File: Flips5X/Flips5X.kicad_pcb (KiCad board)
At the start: 2 copper layers, 80 x 75 mm, 13 parts, among them CN1 Conn_02x30_Odd_Even, CN2 UFP2810, CN3 UFP2810, U1 FP2800A, U2 FP2800A

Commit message: introducing Flips5X concept
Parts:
- added C3: 0U1, Capacitors_SMD:C_0805_HandSoldering, F.Cu at (142.9, 130.2)
- added CNX1: UFP2810, Own:Pin_Header_Angle_Shrouded_2x05_Pitch2.54mm, F.Cu at (152.4, 144.8)
- added CNX2: Conn_02x20_Odd_Even, Socket_Strips:Socket_Strip_Straight_2x20_Pitch2.54mm, B.Cu at (159.4, 88.3)
- added U3: FP2800A, Housings_DIP:DIP-40_W15.24mm_Socket, F.Cu at (139.1, 89.5)
- moved REF** 80.5 mm to (221.1, 112.2)
- moved REF** 74.4 mm to (209.6, 141.0)
- moved REF*** 54.2 mm to (196.8, 131.4)
- moved REF** 40.3 mm to (168.9, 178.4)
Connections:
- net Net-(CN1-Pad1) renamed /SY1
- net Net-(CN1-Pad10) renamed /SY10
- net Net-(CN1-Pad11) renamed /SY11
- net Net-(CN1-Pad12) renamed /SY12
- net Net-(CN1-Pad13) renamed /SY13
- net Net-(CN1-Pad14) renamed /SY14
- net Net-(CN1-Pad15) renamed /SY15
- net Net-(CN1-Pad16) renamed /SY16
- net Net-(CN1-Pad17) renamed /SY17
- net Net-(CN1-Pad18) renamed /SY18
- net Net-(CN1-Pad19) renamed /SY19
- net Net-(CN1-Pad2) renamed /SY2
- net Net-(CN1-Pad20) renamed /SY20
- net Net-(CN1-Pad21) renamed /RY1
- net Net-(CN1-Pad22) renamed /RY2
- net Net-(CN1-Pad23) renamed /RY3
- net Net-(CN1-Pad24) renamed /RY4
- net Net-(CN1-Pad25) renamed /RY5
- net Net-(CN1-Pad26) renamed /RY6
- net Net-(CN1-Pad27) renamed /RY7
- net Net-(CN1-Pad28) renamed /RY8
- net Net-(CN1-Pad29) renamed /RY9
- net Net-(CN1-Pad3) renamed /SY3
- net Net-(CN1-Pad30) renamed /RY10
- net Net-(CN1-Pad31) renamed /RY11
- net Net-(CN1-Pad32) renamed /RY12
- net Net-(CN1-Pad33) renamed /RY13
- net Net-(CN1-Pad34) renamed /RY14
- net Net-(CN1-Pad35) renamed /RY15
- net Net-(CN1-Pad36) renamed /RY16
- net Net-(CN1-Pad37) renamed /RY17
- net Net-(CN1-Pad38) renamed /RY18
- net Net-(CN1-Pad39) renamed /RY19
- net Net-(CN1-Pad4) renamed /SY4
- net Net-(CN1-Pad40) renamed /RY20
- net Net-(CN1-Pad5) renamed /SY5
- net Net-(CN1-Pad6) renamed /SY6
- net Net-(CN1-Pad7) renamed /SY7
- net Net-(CN1-Pad8) renamed /SY8
- net Net-(CN1-Pad9) renamed /SY9
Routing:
- net /X3: track 0.00 -> 20.8 mm
- net /X14: track 0.00 -> 20.8 mm
- net /X1: track 0.00 -> 20.8 mm
- net /X9: track 0.00 -> 20.8 mm
- net /X8: track 0.00 -> 20.8 mm
- net /X7: track 0.00 -> 20.8 mm
- net /X6: track 0.00 -> 20.8 mm
- net /X5: track 0.00 -> 20.8 mm
- net /X4: track 0.00 -> 20.8 mm
- net /X2: track 0.00 -> 20.8 mm
- net /X13: track 0.00 -> 20.8 mm
- net /X12: track 0.00 -> 20.8 mm
- net /X11: track 0.00 -> 20.8 mm
- net /X10: track 0.00 -> 20.8 mm
- net /X23: track 0.00 -> 8.78 mm
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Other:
- board size 80 x 75 mm -> 97 x 75 mm

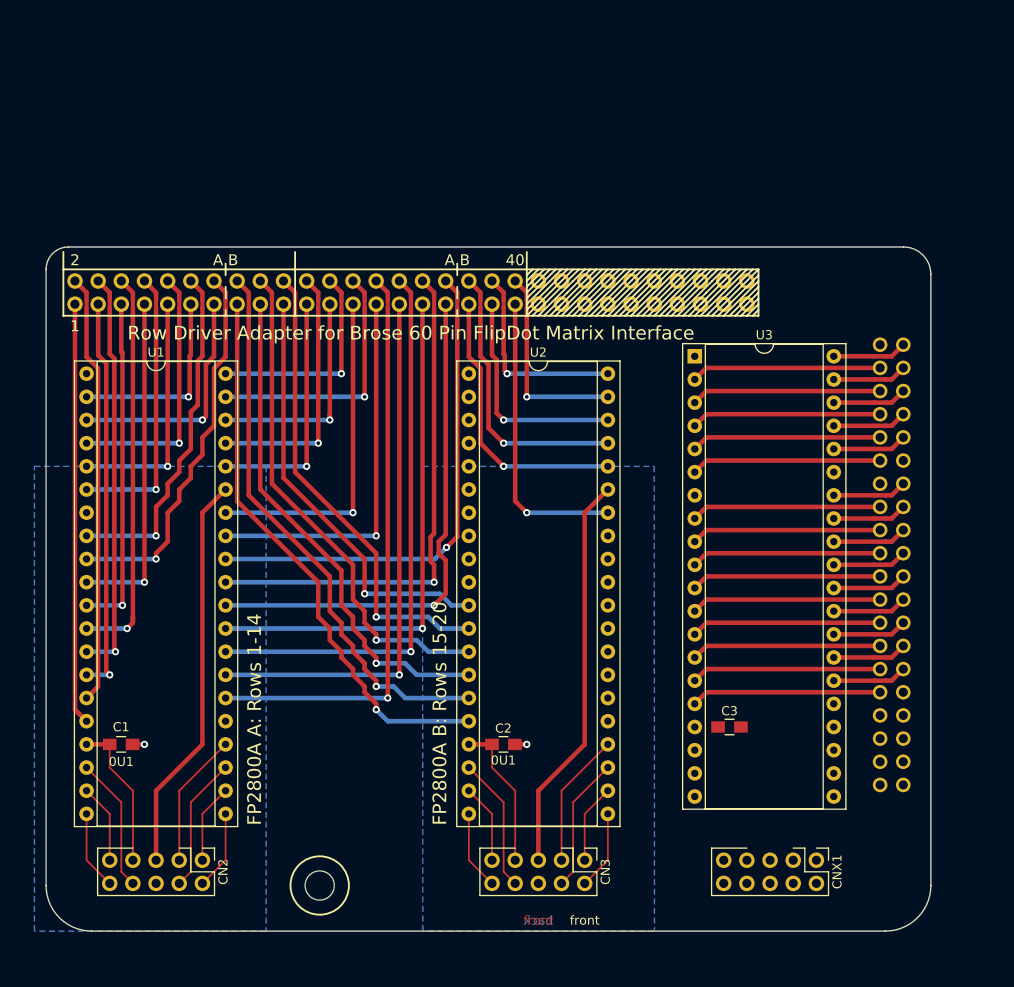
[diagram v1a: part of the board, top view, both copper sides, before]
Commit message: making board 10x10
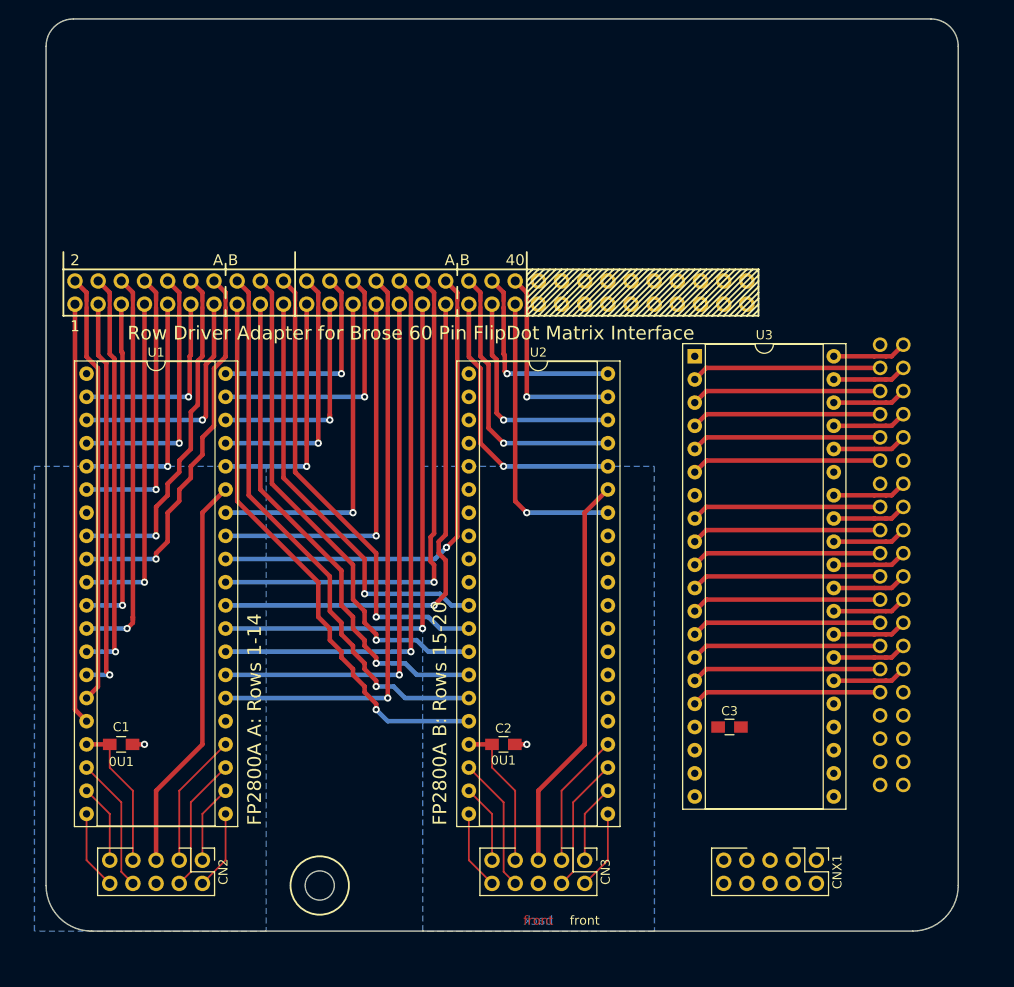
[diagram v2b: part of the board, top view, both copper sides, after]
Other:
- board size 97 x 75 mm -> 100 x 100 mm

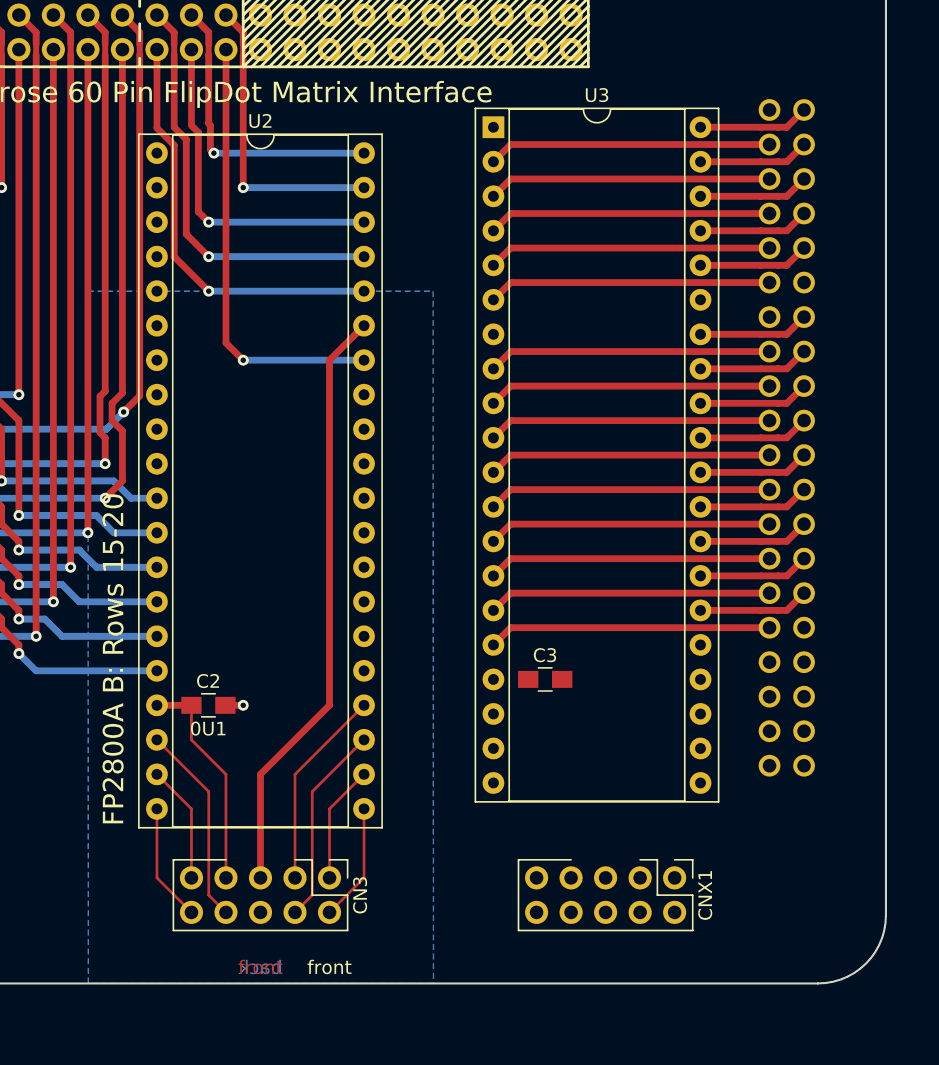
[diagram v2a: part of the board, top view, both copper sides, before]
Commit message: Using new 34P IDC connector for connecting column driver FP2800 onto display board
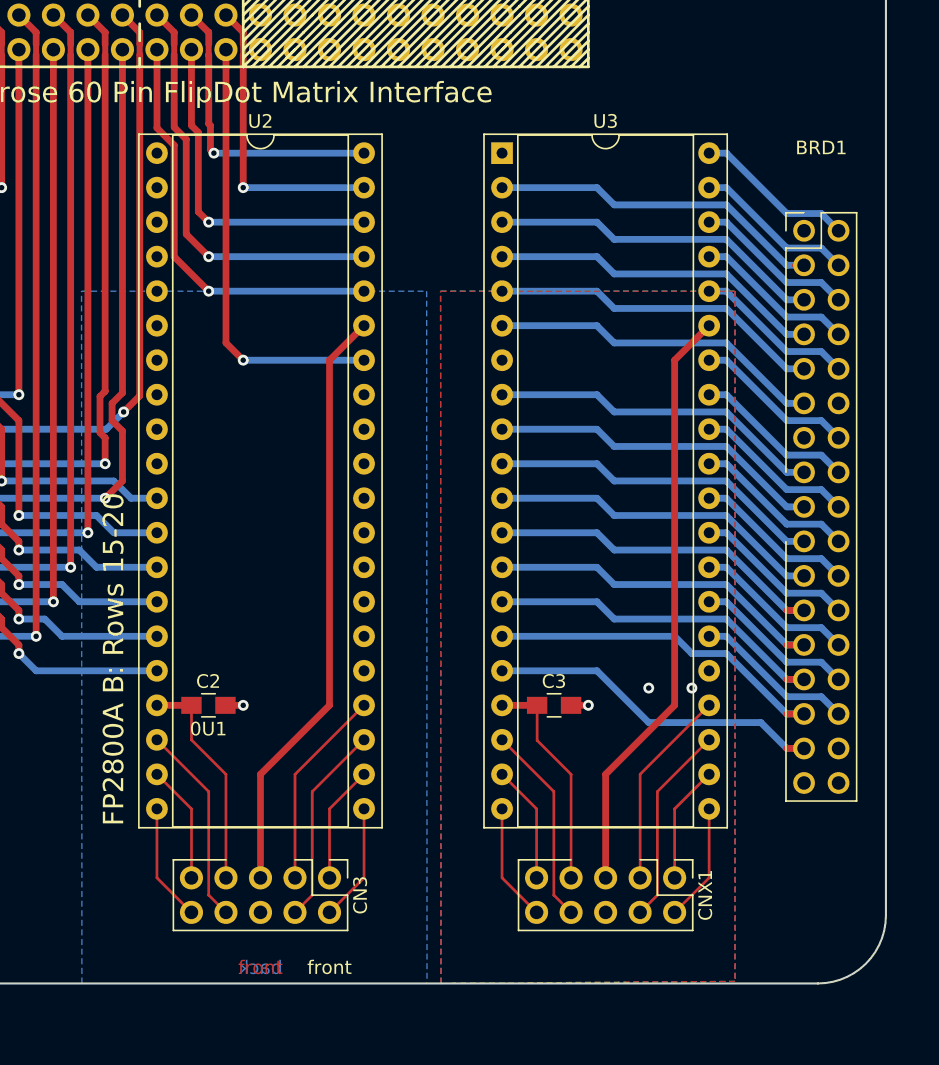
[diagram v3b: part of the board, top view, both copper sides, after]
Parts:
- removed CNX2: Conn_02x20_Odd_Even, Socket_Strips:Socket_Strip_Straight_2x20_Pitch2.54mm
- added BRD1: Conn_02x17_Odd_Even, Own:Pin_Header_Angle_Shrouded_2x17_Pitch2.54mm_ConvNumbering, F.Cu at (161.9, 97.2)
- moved C3 2.01 mm to (143.5, 132.1)
- moved U3 2.01 mm to (139.7, 91.4)
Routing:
- net /X.HV: track 0.00 -> 43.8 mm
- net /X.VCC: track 0.00 -> 16.3 mm
- net /X.A1: track 0.00 -> 14.8 mm
- net /X.POL: track 0.00 -> 14.8 mm
- net /X.EN: track 0.00 -> 14.8 mm
- net /X.A2: track 0.00 -> 8.67 mm
- net /X.A0: track 0.00 -> 8.67 mm
- net /X.B1: track 0.00 -> 8.67 mm
- net /X.B0: track 0.00 -> 8.67 mm
- net /X2: track 20.8 -> 25.9 mm
- net /X6: track 20.8 -> 25.9 mm
- net /X3: track 20.8 -> 25.9 mm
- net /X4: track 20.8 -> 25.9 mm
- net /X1: track 20.8 -> 25.9 mm
- net /X11: track 20.8 -> 25.2 mm
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- added copper zone on B.Cu, net /X.GND
- added copper zone on F.Cu, net /X.GND

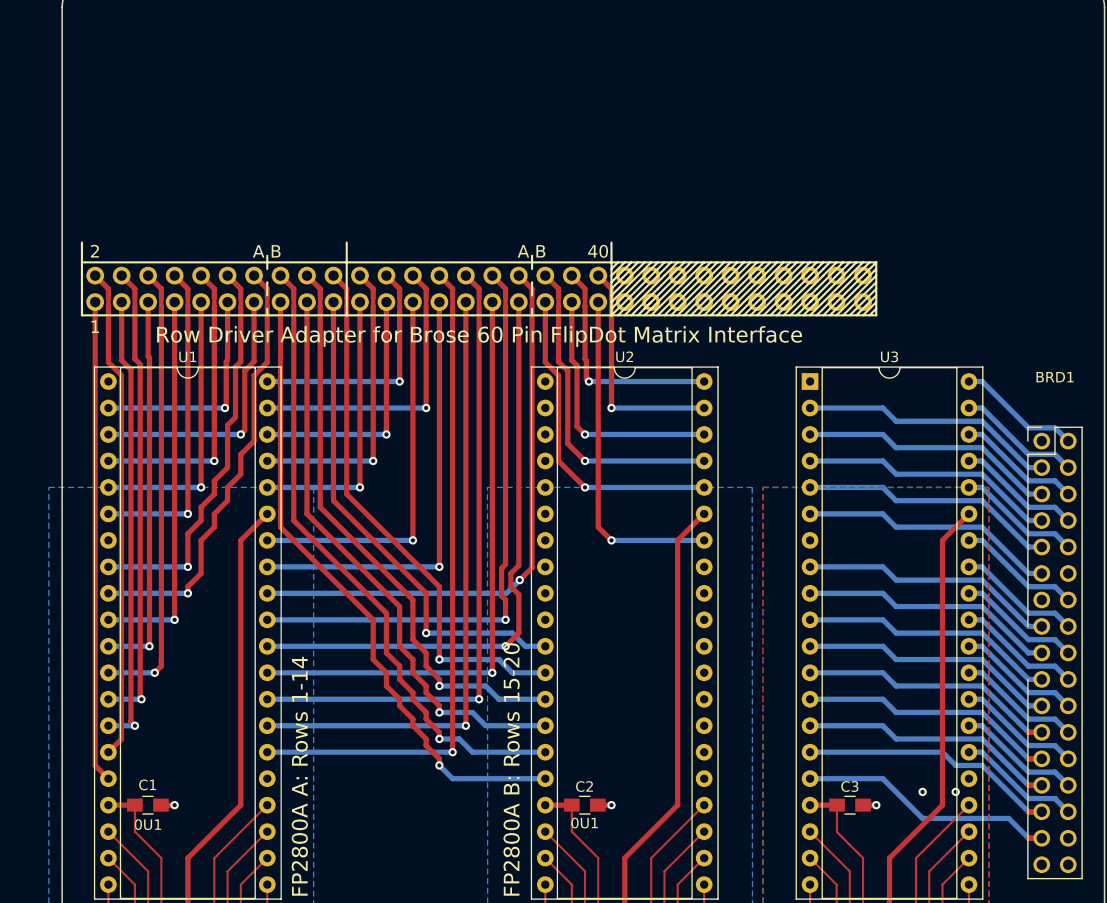
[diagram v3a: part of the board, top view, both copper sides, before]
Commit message: adding 34P connector for 5x digit a 5x7 dots display
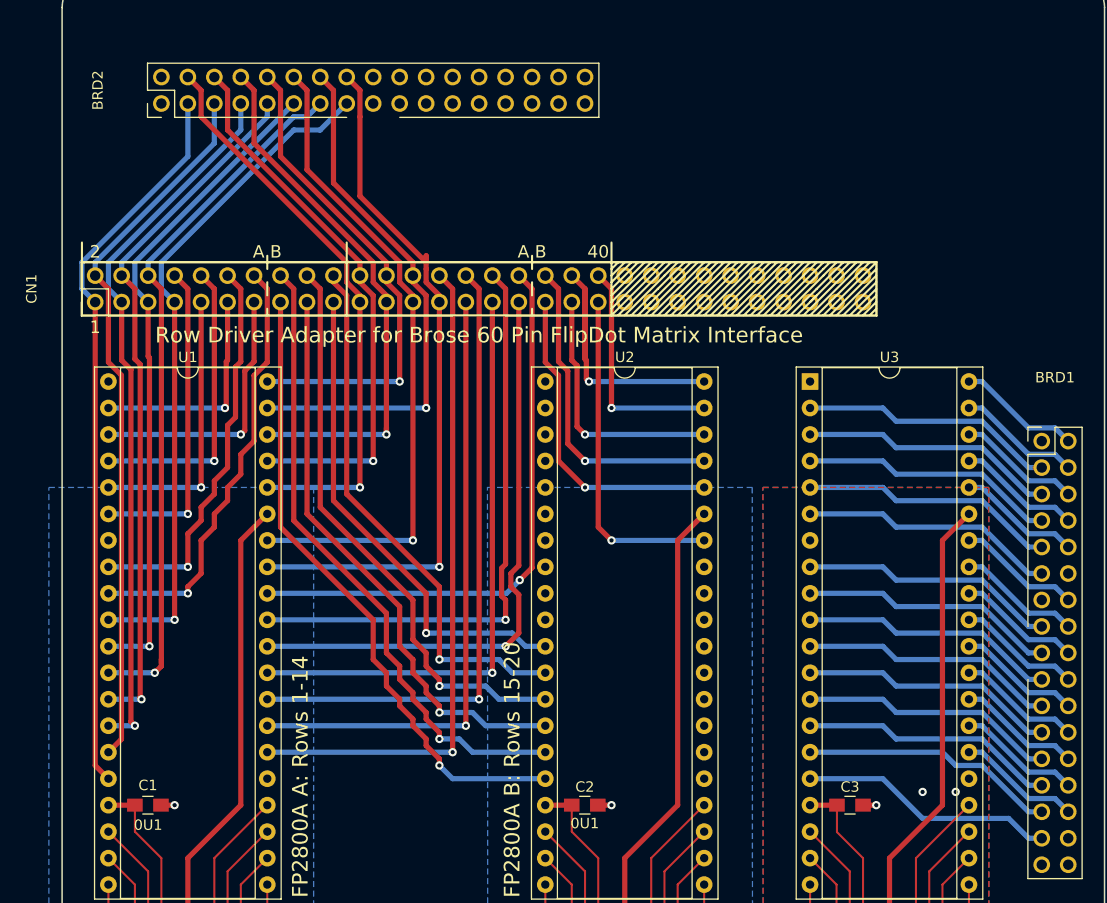
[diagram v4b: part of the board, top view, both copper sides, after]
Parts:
- added BRD2: Conn_02x17_Odd_Even, Own:Pin_Header_Angle_Shrouded_2x17_Pitch2.54mm_ConvNumbering, F.Cu at (77.5, 64.8)
- CN1: footprint Socket_Strips:Socket_Strip_Straight_2x30_Pitch2.54mm -> Own:Pin_Header_Straight_Shrouded_2x30_Pitch2.54mm_ConvNumbering; moved to F.Cu
- turned CN1 to 90 degrees
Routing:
- net /RY1: track 26.7 -> 55.1 mm
- net /SY7: track 36.8 -> 65.3 mm
- net /RY3: track 24.8 -> 52.1 mm
- net /RY7: track 41.9 -> 68.5 mm
- net /RY5: track 36.8 -> 63.2 mm
- net /SY5: track 37.0 -> 62.9 mm
- net /SY3: track 43.7 -> 68.5 mm
- net /RY2: track 28.5 -> 53.3 mm
- net /SY6: track 43.7 -> 67.8 mm
- net /SY1: track 46.2 -> 70.0 mm
- net /RY4: track 23.4 -> 47.2 mm
- net /RY6: track 28.5 -> 51.2 mm
- net /SY4: track 44.6 -> 66.9 mm
- net /SY2: track 47.3 -> 68.5 mm
- net /RY18: track 21.9 -> 28.6 mm
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
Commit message: new layout for FlipsX5
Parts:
- removed the REF** at (221.1, 112.2)
- removed the REF** at (98.0, 147.6)
- removed the REF** at (168.9, 178.4)
- added REF**: MountingHole_3.2mm_M3, Mounting_Holes:MountingHole_3.2mm_M3, F.Cu at (55.8, 145.8)
- added REF**: MountingHole_3.2mm_M3, Mounting_Holes:MountingHole_3.2mm_M3, F.Cu at (145.8, 145.8)
- added REF**: MountingHole_3.2mm_M3, Mounting_Holes:MountingHole_3.2mm_M3, F.Cu at (145.8, 55.8)
- added REF**: MountingHole_3.2mm_M3, Mounting_Holes:MountingHole_3.2mm_M3, F.Cu at (55.8, 55.8)
- REF***: moved to F.Cu
- moved REF** 97.4 mm to (134.6, 78.7), turned to 0 degrees
- moved REF*** 91.2 mm to (121.9, 79.4), turned to 0 degrees
- moved U2 20.9 mm to (94.0, 86.4)
- moved C2 20.9 mm to (97.8, 127.0)
- moved CN3 20.5 mm to (106.7, 142.2)
- moved BRD1 20.2 mm to (143.5, 88.9)
- moved C3 18.5 mm to (125.7, 127.0)
- moved U3 18.5 mm to (121.9, 86.4)
- moved CNX1 18.0 mm to (134.6, 142.2)
- moved CN1 16.5 mm to (64.8, 68.6)
- moved REF*** 10.2 mm to (115.6, 146.7), turned to 0 degrees
- moved U1 8.13 mm to (66.0, 86.4)
- moved C1 8.12 mm to (69.8, 127.0)
- moved BRD2 7.41 mm to (81.3, 58.4)
- moved CN2 6.84 mm to (78.7, 142.2)
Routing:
- net /SY6: track 67.8 -> 111.4 mm, vias 1 -> 0
- net /SY7: track 65.3 -> 106.3 mm, vias 1 -> 0
- net /SY2: track 68.5 -> 103.8 mm
- net /SY5: track 62.9 -> 98.0 mm
- net /SY3: track 68.5 -> 97.7 mm, vias 1 -> 0
- net /SY4: track 66.9 -> 90.0 mm, vias 1 -> 0
- net /SY1: track 70.0 -> 92.8 mm
- net /RY6: track 51.2 -> 66.8 mm
- net /SY8: track 31.0 -> 43.1 mm, vias 1 -> 0
- net /RY5: track 63.2 -> 75.2 mm
- net /SY14: track 41.8 -> 52.2 mm
- net /RY14: track 55.0 -> 64.9 mm
- net /RY9: track 59.7 -> 68.8 mm
- net /RY8: track 64.0 -> 72.8 mm
- net /RY10: track 61.5 -> 70.2 mm
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- added copper zone on F.Cu, net /L.GND
- added copper zone on F.Cu, net /R.GND
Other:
- outline, holes or cut-outs redrawn
- board text added: "Brose 60 Pin FlipDot Matrix Interface Row Driver with Column Driver Port"
- board text added: "FP2800A X: Columns 1-28"
- board text added: "FP2800A Y-1: Rows 1-14"
- board text added: "FP2800A Y-2: Rows 15-20 (optional)"
- board text added: "SRT Flips 5X V1.0 2018-11-10 github.com/cawapy/FlipSuite"
- board text added: "Y-1 Y-2"
- board text removed: "A B"
- board text removed: "FP2800A A: Rows 1-14"
- board text removed: "FP2800A B: Rows 15-20"
- board text removed: "Row Driver Adapter for Brose 60 Pin FlipDot Matrix Interface"
- board text removed: "SRT Flips 5X V1.0 2018-11-02 github.com/cawapy/FlipSuite"
